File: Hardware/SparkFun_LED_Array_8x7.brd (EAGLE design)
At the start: 27.9 x 43.2 mm, 72 parts

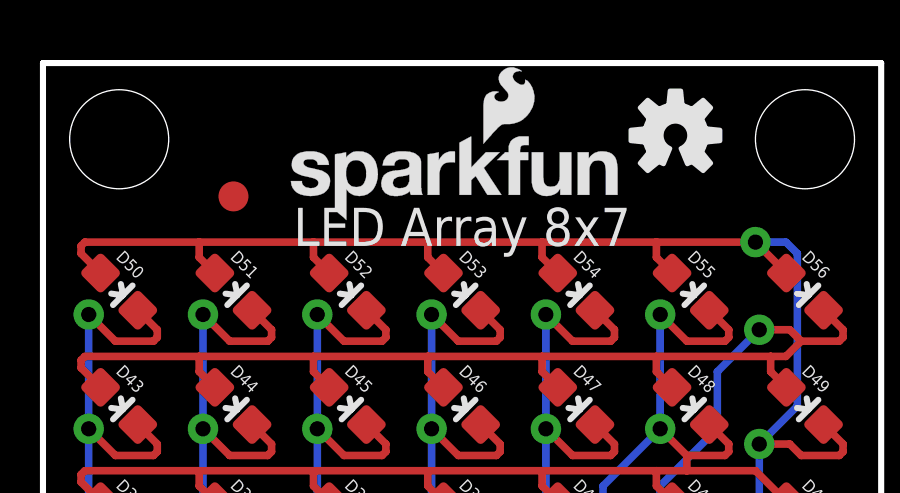
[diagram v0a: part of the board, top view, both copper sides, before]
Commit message: Moved top fiducal and board name silk over to fit under SparkFun logo
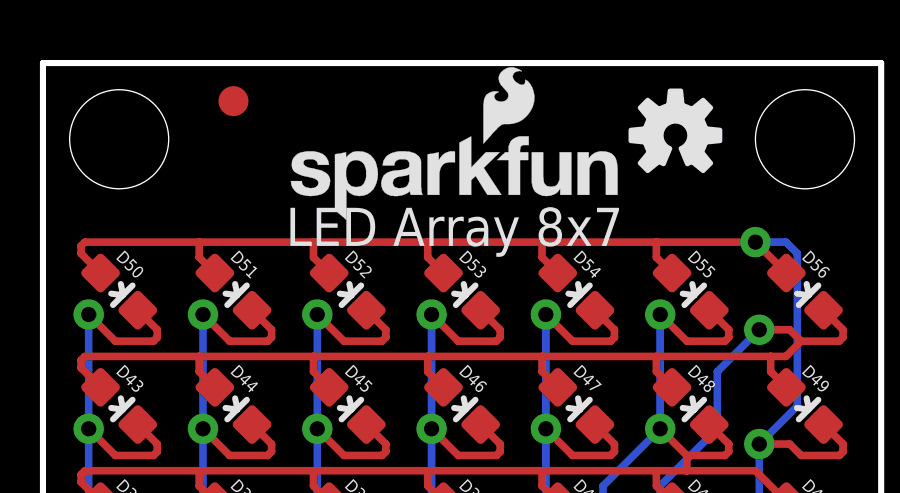
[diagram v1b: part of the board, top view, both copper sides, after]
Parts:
- moved FID2 3.17 mm to (6.35, 41.9)
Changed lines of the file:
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@@
 <setting verticaltext="up"/>
 </settings>
-<grid distance="0.05" unitdist="inch" unit="inch" style="dots" multiple="1" display="yes" altdistance="0.005" altunitdist="inch" altunit="inch"/>
+<grid distance="0.05" unitdist="inch" unit="inch" style="dots" multiple="1" display="yes" altdistance="0.025" altunitdist="inch" altunit="inch"/>
 <layers>
 <layer number="1" name="Top" color="4" fill="1" visible="yes" active="yes"/>
@@
 <wire x1="3.81" y1="0.508" x2="24.13" y2="0.508" width="0.254" layer="22"/>
 <wire x1="3.81" y1="0.254" x2="24.13" y2="0.254" width="0.254" layer="22"/>
-<text x="13.97" y="37.719" size="1.27" layer="21" font="vector" ratio="15" align="center">LED Array 8x7</text>
+<text x="13.716" y="37.719" size="1.27" layer="21" font="vector" ratio="15" align="center">LED Array 8x7</text>
 </plain>
 <attributes>
@@
 </element>
 <element name="FID1" library="SparkFun-Aesthetics" package="FIDUCIAL-1X2" value="FIDUCIAL1X2" x="24.765" y="5.715"/>
-<element name="FID2" library="SparkFun-Aesthetics" package="FIDUCIAL-1X2" value="FIDUCIAL1X2" x="6.35" y="38.735"/>
+<element name="FID2" library="SparkFun-Aesthetics" package="FIDUCIAL-1X2" value="FIDUCIAL1X2" x="6.35" y="41.91"/>
 <element name="FRAME1" library="SparkFun-Aesthetics" package="CREATIVE_COMMONS" value="" x="-11.43" y="-26.67" smashed="yes">
 <attribute name="VERSION" value="v11" x="25.4" y="5.588" size="1.778" layer="16" font="vector" ratio="15" rot="SMR315" align="center"/>

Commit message: Updated library to break up the page template and version number. Printed pdf of schematic.
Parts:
- FRAME1: value (none) -> FRAME-LETTER
- moved FRAME1 9.16 mm to (-19.1, -21.6)
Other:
- board text added: "Shawn Hymel"
- board text added: "v11"
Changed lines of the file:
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@@
 <?xml version="1.0" encoding="utf-8"?>
 <!DOCTYPE eagle SYSTEM "eagle.dtd">
-<eagle version="7.3.0">
+<eagle version="7.2.0">
 <drawing>
 <settings>
@@
 <setting verticaltext="up"/>
 </settings>
-<grid distance="0.05" unitdist="inch" unit="inch" style="dots" multiple="1" display="yes" altdistance="0.025" altunitdist="inch" altunit="inch"/>
+<grid distance="0.05" unitdist="inch" unit="inch" style="dots" multiple="1" display="yes" altdistance="0.005" altunitdist="inch" altunit="inch"/>
 <layers>
 <layer number="1" name="Top" color="4" fill="1" visible="yes" active="yes"/>
@@
 <layer number="45" name="Holes" color="7" fill="1" visible="yes" active="yes"/>
 <layer number="46" name="Milling" color="3" fill="1" visible="no" active="yes"/>
-<layer number="47" name="Measures" color="7" fill="1" visible="yes" active="yes"/>
+<layer number="47" name="Measures" color="7" fill="1" visible="no" active="yes"/>
 <layer number="51" name="tDocu" color="6" fill="1" visible="yes" active="yes"/>
 <layer number="52" name="bDocu" color="7" fill="1" visible="no" active="yes"/>
@@
 <layer number="112" name="tSilk" color="7" fill="1" visible="no" active="no"/>
 <layer number="113" name="IDFDebug" color="4" fill="1" visible="no" active="no"/>
+<layer number="114" name="Badge_Outline" color="7" fill="1" visible="yes" active="yes"/>
+<layer number="115" name="ReferenceISLANDS" color="7" fill="1" visible="yes" active="yes"/>
 <layer number="116" name="Patch_BOT" color="9" fill="4" visible="no" active="no"/>
+<layer number="118" name="Rect_Pads" color="7" fill="1" visible="yes" active="yes"/>
 <layer number="121" name="_tsilk" color="7" fill="1" visible="no" active="no"/>
 <layer number="122" name="_bsilk" color="7" fill="1" visible="no" active="no"/>
@@
 <wire x1="3.81" y1="0.254" x2="24.13" y2="0.254" width="0.254" layer="22"/>
 <text x="13.716" y="37.719" size="1.27" layer="21" font="vector" ratio="15" align="center">LED Array 8x7</text>
+<text x="25.4" y="5.588" size="1.778" layer="16" font="vector" ratio="15" rot="MR135" align="center">v11</text>
+<text x="12.7" y="-21.59" size="1.778" layer="51" font="vector" ratio="15">Shawn Hymel</text>
 </plain>
 <attributes>
@@
 <element name="FID1" library="SparkFun-Aesthetics" package="FIDUCIAL-1X2" value="FIDUCIAL1X2" x="24.765" y="5.715"/>
 <element name="FID2" library="SparkFun-Aesthetics" package="FIDUCIAL-1X2" value="FIDUCIAL1X2" x="6.35" y="41.91"/>
-<element name="FRAME1" library="SparkFun-Aesthetics" package="CREATIVE_COMMONS" value="" x="-11.43" y="-26.67" smashed="yes">
-<attribute name="VERSION" value="v11" x="25.4" y="5.588" size="1.778" layer="16" font="vector" ratio="15" rot="SMR315" align="center"/>
-<attribute name="DESIGNER" value="Shawn Hymel" x="20.32" y="-26.67" size="1.778" layer="51"/>
-</element>
+<element name="FRAME1" library="SparkFun-Aesthetics" package="CREATIVE_COMMONS" value="FRAME-LETTER" x="-19.05" y="-21.59" smashed="yes"/>
 <element name="LOGO2" library="SparkFun-Aesthetics" package="OSHW-LOGO-S" value="OSHW-LOGOS" x="21.082" y="40.767"/>
 <element name="R1" library="SparkFun-Resistors" package="0603-RES" value="82" x="5.08" y="5.08" rot="R90">
 <attribute name="PROD_ID" value="RES-12311" x="5.08" y="5.08" size="1.778" layer="27" rot="R90" display="off"/>
-<attribute name="VALUE" value="82" x="5.08" y="5.08" size="1.778" layer="27" rot="R90" display="off"/>
+<attribute name="VALUE" value="820K" x="5.08" y="5.08" size="1.778" layer="27" rot="R90" display="off"/>
 </element>
 <element name="R2" library="SparkFun-Resistors" package="0603-RES" value="82" x="7.62" y="5.08" rot="R90">
 <attribute name="PROD_ID" value="RES-12311" x="7.62" y="5.08" size="1.778" layer="27" rot="R90" display="off"/>
-<attribute name="VALUE" value="82" x="7.62" y="5.08" size="1.778" layer="27" rot="R90" display="off"/>
+<attribute name="VALUE" value="820K" x="7.62" y="5.08" size="1.778" layer="27" rot="R90" display="off"/>
 </element>
 <element name="R3" library="SparkFun-Resistors" package="0603-RES" value="82" x="10.16" y="5.08" rot="R90">
 <attribute name="PROD_ID" value="RES-12311" x="10.16" y="5.08" size="1.778" layer="27" rot="R90" display="off"/>
-<attribute name="VALUE" value="82" x="10.16" y="5.08" size="1.778" layer="27" rot="R90" display="off"/>
+<attribute name="VALUE" value="820K" x="10.16" y="5.08" size="1.778" layer="27" rot="R90" display="off"/>
 </element>
 <element name="R4" library="SparkFun-Resistors" package="0603-RES" value="82" x="12.7" y="5.08" rot="R90">
 <attribute name="PROD_ID" value="RES-12311" x="12.7" y="5.08" size="1.778" layer="27" rot="R90" display="off"/>
-<attribute name="VALUE" value="82" x="12.7" y="5.08" size="1.778" layer="27" rot="R90" display="off"/>
+<attribute name="VALUE" value="820K" x="12.7" y="5.08" size="1.778" layer="27" rot="R90" display="off"/>
 </element>
 <element name="R5" library="SparkFun-Resistors" package="0603-RES" value="82" x="15.24" y="5.08" rot="R90">
 <attribute name="PROD_ID" value="RES-12311" x="15.24" y="5.08" size="1.778" layer="27" rot="R90" display="off"/>
-<attribute name="VALUE" value="82" x="15.24" y="5.08" size="1.778" layer="27" rot="R90" display="off"/>
+<attribute name="VALUE" value="820K" x="15.24" y="5.08" size="1.778" layer="27" rot="R90" display="off"/>
 </element>
 <element name="R6" library="SparkFun-Resistors" package="0603-RES" value="82" x="17.78" y="5.08" rot="R90">
 <attribute name="PROD_ID" value="RES-12311" x="17.78" y="5.08" size="1.778" layer="27" rot="R90" display="off"/>
-<attribute name="VALUE" value="82" x="17.78" y="5.08" size="1.778" layer="27" rot="R90" display="off"/>
+<attribute name="VALUE" value="820K" x="17.78" y="5.08" size="1.778" layer="27" rot="R90" display="off"/>
 </element>
 <element name="R7" library="SparkFun-Resistors" package="0603-RES" value="82" x="20.32" y="5.08" rot="R90">
 <attribute name="PROD_ID" value="RES-12311" x="20.32" y="5.08" size="1.778" layer="27" rot="R90" display="off"/>
-<attribute name="VALUE" value="82" x="20.32" y="5.08" size="1.778" layer="27" rot="R90" display="off"/>
+<attribute name="VALUE" value="820K" x="20.32" y="5.08" size="1.778" layer="27" rot="R90" display="off"/>
 </element>
 <element name="R8" library="SparkFun-Resistors" package="0603-RES" value="82" x="22.86" y="5.08" rot="R90">
 <attribute name="PROD_ID" value="RES-12311" x="22.86" y="5.08" size="1.778" layer="27" rot="R90" display="off"/>
-<attribute name="VALUE" value="82" x="22.86" y="5.08" size="1.778" layer="27" rot="R90" display="off"/>
+<attribute name="VALUE" value="820K" x="22.86" y="5.08" size="1.778" layer="27" rot="R90" display="off"/>
 </element>
 <element name="STANDOFF1" library="SparkFun-Electromechanical" package="STAND-OFF" value="STAND-OFF" x="25.4" y="40.64" rot="R90"/>
